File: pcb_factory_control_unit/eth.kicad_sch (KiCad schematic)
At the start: 27 parts, among them U2 LAN8742A, Y1 25MHz

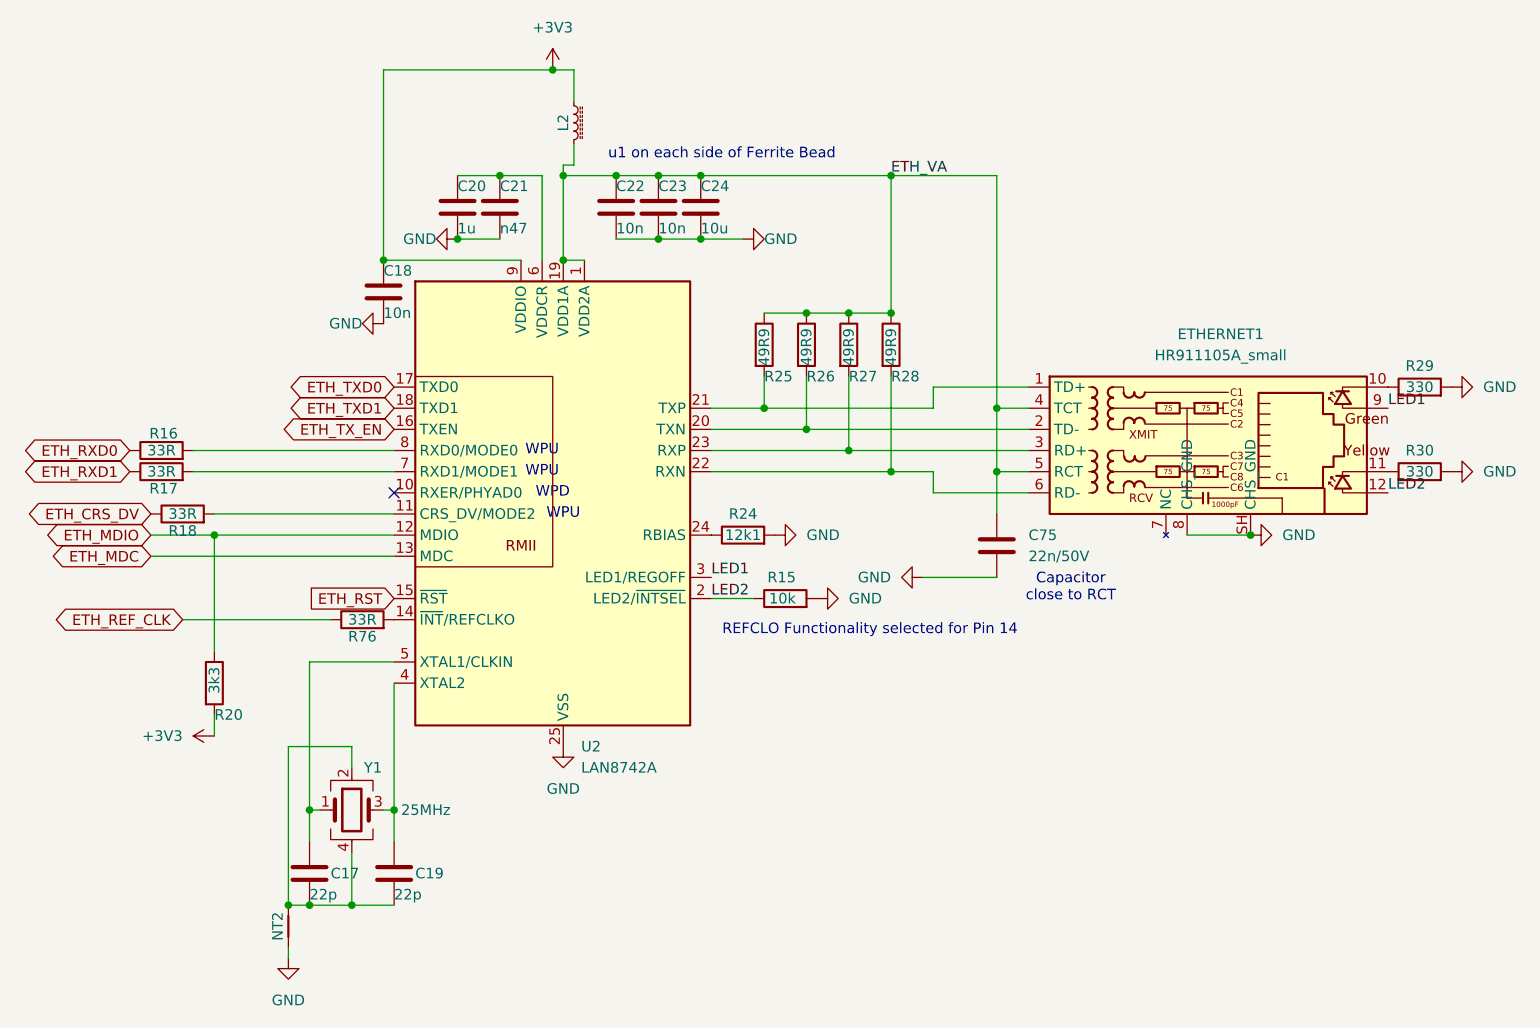
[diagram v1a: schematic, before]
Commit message: Control Unit PCB: schematic rework (PSU, MX26631DL, XL6009 module, ERC fixes), new placement on 90 mm high board
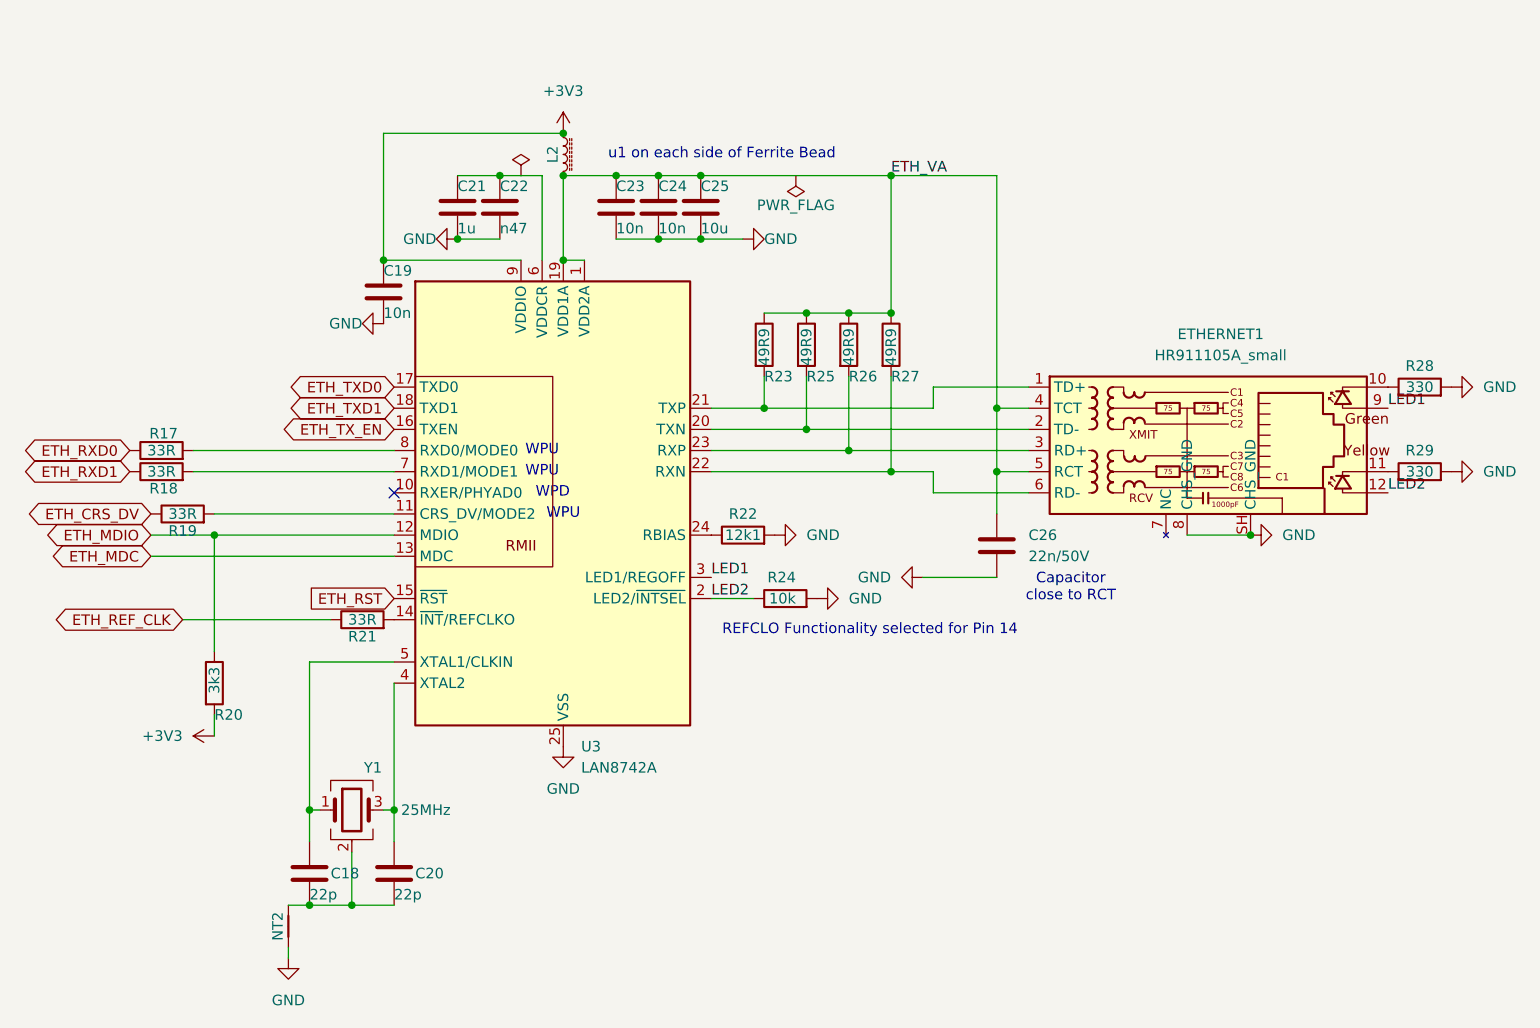
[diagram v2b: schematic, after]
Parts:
- renumbered C17 to C18, C18 to C19, C19 to C20, C20 to C21, C21 to C22, C22 to C23, C23 to C24, C24 to C25, C75 to C26, R16 to R17, R17 to R18, R18 to R19, R76 to R21, R24 to R22, R25 to R23, R15 to R24, R26 to R25, R27 to R26, R28 to R27, R29 to R28, R30 to R29, U2 to U3
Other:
- moved on the sheet: L2

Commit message: PCB WIP
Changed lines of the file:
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@@
 	(global_label "ETH_TXD0"
 		(shape bidirectional)
-		(at 85.09 62.23 180)
+		(at 85.09 62.23 0)
 		(fields_autoplaced yes)
 		(effects
@@
 				(size 1.27 1.27)
 			)
-			(justify right)
+			(justify left)
 		)
 		(property "Intersheetrefs" "${INTERSHEET_REFS}"
-			(at 71.9222 62.23 0)
+			(at 98.2578 62.23 0)
 			(hide yes)
 			(show_name no)
@@
 					(size 1.27 1.27)
 				)
-				(justify right)
+				(justify left)
 			)
 		)
@@
 	(global_label "ETH_MDC"
 		(shape bidirectional)
-		(at 55.88 82.55 180)
+		(at 55.88 82.55 0)
 		(fields_autoplaced yes)
 		(effects
@@
 				(size 1.27 1.27)
 			)
-			(justify right)
+			(justify left)
 		)
 		(property "Intersheetrefs" "${INTERSHEET_REFS}"
-			(at 43.3774 82.55 0)
+			(at 68.3826 82.55 0)
 			(hide yes)
 			(show_name no)
@@
 					(size 1.27 1.27)
 				)
-				(justify right)
+				(justify left)
 			)
 		)

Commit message: PCB WIP
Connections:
- net GND: no longer ETHERNET1.8 (CHS_GND), ETHERNET1.SH (CHS_GND)
- new net GND1: ETHERNET1.8 (CHS_GND), ETHERNET1.SH (CHS_GND)
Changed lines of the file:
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@@
 	(global_label "ETH_TXD0"
 		(shape bidirectional)
-		(at 85.09 62.23 0)
+		(at 85.09 62.23 180)
 		(fields_autoplaced yes)
 		(effects
@@
 				(size 1.27 1.27)
 			)
-			(justify left)
+			(justify right)
 		)
 		(property "Intersheetrefs" "${INTERSHEET_REFS}"
-			(at 98.2578 62.23 0)
-			(hide yes)
-			(show_name no)
-			(do_not_autoplace no)
-			(effects
-				(font
-					(size 1.27 1.27)
-				)
-				(justify left)
+			(at 71.9222 62.23 0)
+			(hide yes)
+			(show_name no)
+			(do_not_autoplace no)
+			(effects
+				(font
+					(size 1.27 1.27)
+				)
+				(justify right)
 			)
 		)
@@
 	)
 	(symbol
-		(lib_id "power:GND")
-		(at 187.96 80.01 90)
-		(unit 1)
-		(body_style 1)
-		(exclude_from_sim no)
-		(in_bom yes)
-		(on_board yes)
-		(in_pos_files yes)
-		(dnp no)
-		(fields_autoplaced yes)
-		(property "Reference" "#PWR044"
-			(at 194.31 80.01 0)
-			(hide yes)
-			(show_name no)
-			(do_not_autoplace no)
-			(effects
-				(font
-					(size 1.27 1.27)
-				)
-			)
-		)
-		(property "Value" "GND"
-			(at 191.77 80.0099 90)
-			(show_name no)
-			(do_not_autoplace no)
-			(effects
-				(font
-					(size 1.27 1.27)
-				)
-				(justify right)
-			)
-		)
-		(property "Footprint" ""
-			(at 187.96 80.01 0)
-			(hide yes)
-			(show_name no)
-			(do_not_autoplace no)
-			(effects
-				(font
-					(size 1.27 1.27)
-				)
-			)
-		)
-		(property "Datasheet" ""
-			(at 187.96 80.01 0)
-			(hide yes)
-			(show_name no)
-			(do_not_autoplace no)
-			(effects
-				(font
-					(size 1.27 1.27)
-				)
-			)
-		)
-		(property "Description" "Power symbol creates a global label with name \"GND\" , ground"
-			(at 187.96 80.01 0)
-			(hide yes)
-			(show_name no)
-			(do_not_autoplace no)
-			(effects
-				(font
-					(size 1.27 1.27)
-				)
-			)
-		)
-		(pin "1"
-		)
-		(instances
-			(project "pcb_factory_control_unit"
-				(path "/9c57264a-0988-4c94-95c0-340e4ca73bd5/53d03dea-1884-4b59-a05f-593b0c1ac681"
-					(reference "#PWR044")
-					(unit 1)
-				)
-			)
-		)
-	)
-	(symbol
 		(lib_id "Device:R")
 		(at 57.15 72.39 90)
@@
 					(unit 1)
 				)
+			)
+		)
+	)
+	(symbol
+		(lib_id "power:GND1")
+		(at 187.96 80.01 0)
+		(unit 1)
+		(body_style 1)
+		(exclude_from_sim no)
+		(in_bom yes)
+		(on_board yes)
+		(in_pos_files yes)
+		(dnp no)
+		(fields_autoplaced yes)
+		(property "Reference" "#PWR044"
+			(at 187.96 86.36 0)
+			(hide yes)
+			(show_name no)
+			(do_not_autoplace no)
+			(effects
+				(font
+					(size 1.27 1.27)
+				)
+			)
+		)
+		(property "Value" "GND1"
+			(at 187.96 85.09 0)
+			(show_name no)
+			(do_not_autoplace no)
+			(effects
+				(font
+					(size 1.27 1.27)
+				)
+			)
+		)
+		(property "Footprint" ""
+			(at 187.96 80.01 0)
+			(hide yes)
+			(show_name no)
+			(do_not_autoplace no)
+			(effects
+				(font
+					(size 1.27 1.27)
+				)
+			)
+		)
+		(property "Datasheet" ""
+			(at 187.96 80.01 0)
+			(hide yes)
+			(show_name no)
+			(do_not_autoplace no)
+			(effects
+				(font
+					(size 1.27 1.27)
+				)
+			)
+		)
+		(property "Description" "Power symbol creates a global label with name \"GND1\" , ground"
+			(at 187.96 80.01 0)
+			(hide yes)
+			(show_name no)
+			(do_not_autoplace no)
+			(effects
+				(font
+					(size 1.27 1.27)
+				)
+			)
+		)
+		(pin "1"
+		)
+		(instances
+			(project "pcb_factory_control_unit"
+				(path "/9c57264a-0988-4c94-95c0-340e4ca73bd5/53d03dea-1884-4b59-a05f-593b0c1ac681"
+					(reference "#PWR044")
+					(unit 1)
+				)

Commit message: FCB ready for review
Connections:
- net CLK_GND: now reaches C18.2, C20.2, NT2.2, Y1.2 (G), Y1.4 (G)
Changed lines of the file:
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@@
+		)
+	)
+	(label "CLK_GND"
+		(at 72.39 124.46 90)
+		(effects
+			(font
+				(size 1.27 1.27)
+			)
+			(justify left bottom)
 		)
 	)
